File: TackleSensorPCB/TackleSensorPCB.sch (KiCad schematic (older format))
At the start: 26 parts, among them J1 PJ-037A, J2 Conn_01x03_Male, J3 Conn_01x04_Male, J4 Conn_01x07_Male, Q1 2N7002, Q2 2N7002, SW1 SW_DPST_x2, U1 TPS62172DSG, U2 MSP430FR2433IRGER, U3 MMA8452QR1

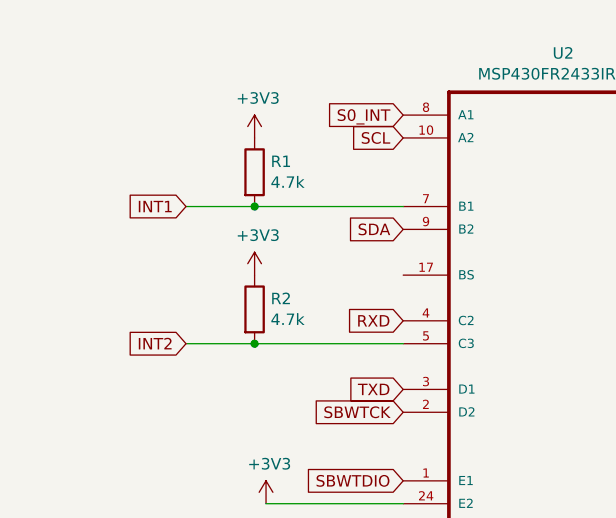
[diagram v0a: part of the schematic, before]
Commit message: Added Footprints
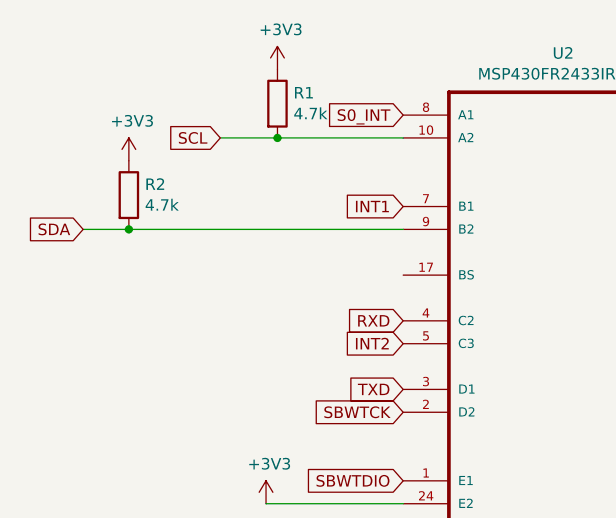
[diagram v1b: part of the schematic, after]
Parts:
- C1, C2, C3, C4, C5: footprint (none) -> Capacitor_SMD:C_0402_1005Metric
- D1: footprint (none) -> LED_SMD:LED_0603_1608Metric
- D2: footprint (none) -> SOD-123FL:SOD123FL
- F1: footprint (none) -> Fuse:Fuse_1206_3216Metric
- J1: footprint CUI_PJ-037A -> PJ-037A:CUI_PJ-037A
- J2: footprint (none) -> Connector_PinHeader_2.54mm:PinHeader_1x03_P2.54mm_Vertical
- J3: footprint (none) -> Connector_PinHeader_2.54mm:PinHeader_1x04_P2.54mm_Vertical
- J4: footprint (none) -> Connector_PinHeader_2.54mm:PinHeader_1x07_P2.54mm_Horizontal
- L1: footprint (none) -> Inductor_SMD:L_0805_2012Metric
- R1, R2, R3, R6, R7: footprint (none) -> Resistor_SMD:R_0402_1005Metric
- R4: footprint (none) -> Resistor_SMD:R_1206_3216Metric
- R5: footprint (none) -> Resistor_SMD:R_0603_1608Metric
- SW1: footprint (none) -> TS-1187A-B-A-B:SW_TS-1187A-B-A-B
- U2: footprint QFN50P400X400X100-25N -> MSP430FR2433:QFN50P400X400X100-25N
- U3: footprint QFN50P300X300X100-16N -> MMA8452QR1:QFN50P300X300X100-16N
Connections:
- net INT1: no longer R1.2
- net INT2: no longer R2.2
- net SCL: now also R1.2
- net SDA: now also R2.2
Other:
- moved on the sheet: R1, R2
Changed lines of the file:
@@
 F 0 "U2" H 2900 3620 50  0000 C CNN
 F 1 "MSP430FR2433IRGER" H 2900 3529 50  0000 C CNN
-F 2 "QFN50P400X400X100-25N" H 2900 2450 50  0001 L BNN
+F 2 "MSP430FR2433:QFN50P400X400X100-25N" H 2900 2450 50  0001 L BNN
 F 3 "" H 2900 2450 50  0001 C CNN
 	1    2900 2450
@@
 F 0 "U3" H 8300 3370 50  0000 C CNN
 F 1 "MMA8452QR1" H 8300 3279 50  0000 C CNN
-F 2 "QFN50P300X300X100-16N" H 8300 2300 50  0001 L BNN
+F 2 "MMA8452QR1:QFN50P300X300X100-16N" H 8300 2300 50  0001 L BNN
 F 3 "Freescale" H 8300 2300 50  0001 L BNN
 F 4 "QFN-16" H 8300 2300 50  0001 L BNN "Field4"
@@
 	1    0    0    -1
 $EndComp
-Text GLabel 1250 2550 0    50   Input ~ 0
+Text GLabel 2200 2550 0    50   Input ~ 0
 INT2
-Text GLabel 1250 1950 0    50   Input ~ 0
+Text GLabel 2200 1950 0    50   Input ~ 0
 INT1
 Text GLabel 2200 1550 0    50   Input ~ 0
 S0_INT
-Text GLabel 2200 2050 0    50   Input ~ 0
+Text GLabel 800  2050 0    50   Input ~ 0
 SDA
-Text GLabel 2200 1650 0    50   Input ~ 0
+Text GLabel 1400 1650 0    50   Input ~ 0
 SCL
 Wire Wire Line
@@
 F 0 "C1" H 2015 4496 50  0000 L CNN
 F 1 "10 uF" H 2015 4405 50  0000 L CNN
-F 2 "" H 1938 4300 50  0001 C CNN
+F 2 "Capacitor_SMD:C_0402_1005Metric" H 1938 4300 50  0001 C CNN
 F 3 "~" H 1900 4450 50  0001 C CNN
 	1    1900 4450
@@
 F 0 "L1" V 3640 4200 50  0000 C CNN
 F 1 "2.2 uH" V 3549 4200 50  0000 C CNN
-F 2 "" H 3450 4200 50  0001 C CNN
+F 2 "Inductor_SMD:L_0805_2012Metric" H 3450 4200 50  0001 C CNN
 F 3 "~" H 3450 4200 50  0001 C CNN
 	1    3450 4200
@@
 F 0 "R3" H 3820 4496 50  0000 L CNN
 F 1 "100k" H 3820 4405 50  0000 L CNN
-F 2 "" V 3680 4450 50  0001 C CNN
+F 2 "Resistor_SMD:R_0402_1005Metric" V 3680 4450 50  0001 C CNN
 F 3 "~" H 3750 4450 50  0001 C CNN
 	1    3750 4450
@@
 INT2
 Wire Wire Line
-	2200 1950 1550 1950
-Wire Wire Line
-	2200 2550 1550 2550
-$Comp
-L Device:R R2
-U 1 1 5F83BDA3
-P 1550 2400
-F 0 "R2" H 1620 2446 50  0000 L CNN
-F 1 "4.7k" H 1620 2355 50  0000 L CNN
-F 2 "" V 1480 2400 50  0001 C CNN
-F 3 "~" H 1550 2400 50  0001 C CNN
-	1    1550 2400
-	1    0    0    -1
-$EndComp
-Connection ~ 1550 2550
-Wire Wire Line
-	1550 2550 1250 2550
+	2200 1650 1650 1650
 $Comp
 L Device:R R1
 U 1 1 5F83C388
-P 1550 1800
-F 0 "R1" H 1620 1846 50  0000 L CNN
-F 1 "4.7k" H 1620 1755 50  0000 L CNN
-F 2 "" V 1480 1800 50  0001 C CNN
-F 3 "~" H 1550 1800 50  0001 C CNN
-	1    1550 1800
-	1    0    0    -1
-$EndComp
-Connection ~ 1550 1950
-Wire Wire Line
-	1550 1950 1250 1950
+P 1650 1500
+F 0 "R1" H 1720 1546 50  0000 L CNN
+F 1 "4.7k" H 1720 1455 50  0000 L CNN
+F 2 "Resistor_SMD:R_0402_1005Metric" V 1580 1500 50  0001 C CNN
+F 3 "~" H 1650 1500 50  0001 C CNN
+	1    1650 1500
+	1    0    0    -1
+$EndComp
 $Comp
 L power:+3V3 #PWR01
 U 1 1 5F83CA3F
-P 1550 1650
-F 0 "#PWR01" H 1550 1500 50  0001 C CNN
-F 1 "+3V3" H 1565 1823 50  0000 C CNN
-F 2 "" H 1550 1650 50  0001 C CNN
-F 3 "" H 1550 1650 50  0001 C CNN
-	1    1550 1650
-	1    0    0    -1
-$EndComp
-$Comp
-L power:+3V3 #PWR02
-U 1 1 5F83D152
-P 1550 2250
-F 0 "#PWR02" H 1550 2100 50  0001 C CNN
-F 1 "+3V3" H 1565 2423 50  0000 C CNN
-F 2 "" H 1550 2250 50  0001 C CNN
-F 3 "" H 1550 2250 50  0001 C CNN
-	1    1550 2250
+P 1650 1350
+F 0 "#PWR01" H 1650 1200 50  0001 C CNN
+F 1 "+3V3" H 1665 1523 50  0000 C CNN
+F 2 "" H 1650 1350 50  0001 C CNN
+F 3 "" H 1650 1350 50  0001 C CNN
+	1    1650 1350
 	1    0    0    -1
 $EndComp
@@
 F 0 "C5" H 7065 2096 50  0000 L CNN
 F 1 "0.1 uF" H 7065 2005 50  0000 L CNN
-F 2 "" H 6988 1900 50  0001 C CNN
+F 2 "Capacitor_SMD:C_0402_1005Metric" H 6988 1900 50  0001 C CNN
 F 3 "~" H 6950 2050 50  0001 C CNN
 	1    6950 2050
@@
 F 0 "D1" V 7939 5932 50  0000 R CNN
 F 1 "LED" V 7848 5932 50  0000 R CNN
-F 2 "" H 7900 6050 50  0001 C CNN
+F 2 "LED_SMD:LED_0603_1608Metric" H 7900 6050 50  0001 C CNN
 F 3 "~" H 7900 6050 50  0001 C CNN
 	1    7900 6050
@@
 F 0 "SW1" H 7700 5535 50  0000 C CNN
 F 1 "SW_DPST_x2" H 7700 5444 50  0000 C CNN
-F 2 "" H 7700 5300 50  0001 C CNN
+F 2 "TS-1187A-B-A-B:SW_TS-1187A-B-A-B" H 7700 5300 50  0001 C CNN
 F 3 "~" H 7700 5300 50  0001 C CNN
 	1    7700 5300
@@
 F 0 "R5" V 7493 4800 50  0000 C CNN
 F 1 "330" V 7584 4800 50  0000 C CNN
-F 2 "" V 7630 4800 50  0001 C CNN
+F 2 "Resistor_SMD:R_0603_1608Metric" V 7630 4800 50  0001 C CNN
 F 3 "~" H 7700 4800 50  0001 C CNN
 	1    7700 4800
@@
 F 0 "J2" H 9908 4331 50  0000 C CNN
 F 1 "Conn_01x03_Male" H 9908 4240 50  0000 C CNN
-F 2 "" H 9800 4050 50  0001 C CNN
+F 2 "Connector_PinHeader_2.54mm:PinHeader_1x03_P2.54mm_Vertical" H 9800 4050 50  0001 C CNN
 F 3 "~" H 9800 4050 50  0001 C CNN
 	1    9800 4050
@@
 F 0 "J4" H 9908 6331 50  0000 C CNN
 F 1 "Conn_01x07_Male" H 9908 6240 50  0000 C CNN
-F 2 "" H 9800 5850 50  0001 C CNN
+F 2 "Connector_PinHeader_2.54mm:PinHeader_1x07_P2.54mm_Horizontal" H 9800 5850 50  0001 C CNN
 F 3 "~" H 9800 5850 50  0001 C CNN
 	1    9800 5850
@@
 F 0 "J1" H 7545 4490 50  0000 C CNN
 F 1 "PJ-037A" H 7545 4399 50  0000 C CNN
-F 2 "CUI_PJ-037A" H 7550 4150 50  0001 L BNN
+F 2 "PJ-037A:CUI_PJ-037A" H 7550 4150 50  0001 L BNN
 F 3 "Manufacturer recommendations" H 7550 4150 50  0001 L BNN
 F 4 "CUI INC" H 7550 4150 50  0001 L BNN "Field4"
@@
 F 0 "R6" H 2870 6096 50  0000 L CNN
 F 1 "4.7k" H 2870 6005 50  0000 L CNN
-F 2 "" V 2730 6050 50  0001 C CNN
+F 2 "Resistor_SMD:R_0402_1005Metric" V 2730 6050 50  0001 C CNN
 F 3 "~" H 2800 6050 50  0001 C CNN
 	1    2800 6050
@@
 F 0 "R7" H 3770 6096 50  0000 L CNN
 F 1 "4.7k" H 3770 6005 50  0000 L CNN
-F 2 "" V 3630 6050 50  0001 C CNN
+F 2 "Resistor_SMD:R_0402_1005Metric" V 3630 6050 50  0001 C CNN
 F 3 "~" H 3700 6050 50  0001 C CNN
 	1    3700 6050
@@
 F 0 "R4" H 7670 6096 50  0000 L CNN
 F 1 "100" H 7670 6005 50  0000 L CNN
-F 2 "" V 7530 6050 50  0001 C CNN
+F 2 "Resistor_SMD:R_1206_3216Metric" V 7530 6050 50  0001 C CNN
 F 3 "~" H 7600 6050 50  0001 C CNN
 	1    7600 6050
@@
 F 0 "C2" H 4315 4496 50  0000 L CNN
 F 1 "10uF" H 4315 4405 50  0000 L CNN
-F 2 "" H 4238 4300 50  0001 C CNN
+F 2 "Capacitor_SMD:C_0402_1005Metric" H 4238 4300 50  0001 C CNN
 F 3 "~" H 4200 4450 50  0001 C CNN
 	1    4200 4450
@@
 F 0 "C3" H 4765 4496 50  0000 L CNN
 F 1 "10uF" H 4765 4405 50  0000 L CNN
-F 2 "" H 4688 4300 50  0001 C CNN
+F 2 "Capacitor_SMD:C_0402_1005Metric" H 4688 4300 50  0001 C CNN
 F 3 "~" H 4650 4450 50  0001 C CNN
 	1    4650 4450
@@
 F 0 "C4" H 5215 4496 50  0000 L CNN
 F 1 "10uF" H 5215 4405 50  0000 L CNN
-F 2 "" H 5138 4300 50  0001 C CNN
+F 2 "Capacitor_SMD:C_0402_1005Metric" H 5138 4300 50  0001 C CNN
 F 3 "~" H 5100 4450 50  0001 C CNN
 	1    5100 4450
@@
 F 0 "F1" H 1300 4385 50  0000 C CNN
 F 1 "Fuse_Small" H 1300 4294 50  0000 C CNN
-F 2 "" H 1300 4200 50  0001 C CNN
+F 2 "Fuse:Fuse_1206_3216Metric" H 1300 4200 50  0001 C CNN
 F 3 "~" H 1300 4200 50  0001 C CNN
 	1    1300 4200
@@
 F 0 "D2" V 1504 4480 50  0000 L CNN
 F 1 "D" V 1595 4480 50  0000 L CNN
-F 2 "" H 1550 4400 50  0001 C CNN
+F 2 "SOD-123FL:SOD123FL" H 1550 4400 50  0001 C CNN
 F 3 "~" H 1550 4400 50  0001 C CNN
 	1    1550 4400
@@
 F 0 "J3" H 9908 5081 50  0000 C CNN
 F 1 "Conn_01x04_Male" H 9908 4990 50  0000 C CNN
-F 2 "" H 9800 4800 50  0001 C CNN
+F 2 "Connector_PinHeader_2.54mm:PinHeader_1x04_P2.54mm_Vertical" H 9800 4800 50  0001 C CNN
 F 3 "~" H 9800 4800 50  0001 C CNN
 	1    9800 4800
@@
 $EndComp
 $Comp
-L power:GND #PWR?
+L power:GND #PWR0101
 U 1 1 5F86DE04
 P 6950 2200
-F 0 "#PWR?" H 6950 1950 50  0001 C CNN
+F 0 "#PWR0101" H 6950 1950 50  0001 C CNN
 F 1 "GND" H 6955 2027 50  0000 C CNN
 F 2 "" H 6950 2200 50  0001 C CNN
@@
 	1    0    0    -1
 $EndComp
+$Comp
+L power:+3V3 #PWR02
+U 1 1 5F83D152
+P 1000 1750
+F 0 "#PWR02" H 1000 1600 50  0001 C CNN
+F 1 "+3V3" H 1015 1923 50  0000 C CNN
+F 2 "" H 1000 1750 50  0001 C CNN
+F 3 "" H 1000 1750 50  0001 C CNN
+	1    1000 1750
+	1    0    0    -1
+$EndComp
+$Comp
+L Device:R R2
+U 1 1 5F83BDA3
+P 1000 1900
+F 0 "R2" H 1070 1946 50  0000 L CNN
+F 1 "4.7k" H 1070 1855 50  0000 L CNN
+F 2 "Resistor_SMD:R_0402_1005Metric" V 930 1900 50  0001 C CNN
+F 3 "~" H 1000 1900 50  0001 C CNN
+	1    1000 1900
+	1    0    0    -1
+$EndComp
+Connection ~ 1000 2050
+Wire Wire Line
+	1000 2050 2200 2050
+Wire Wire Line
+	800  2050 1000 2050
+Wire Wire Line
+	1400 1650 1650 1650
+Connection ~ 1650 1650
 $EndSCHEMATC

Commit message: Created First Revision of PCB
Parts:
- J4: footprint Connector_PinHeader_2.54mm:PinHeader_1x07_P2.54mm_Horizontal -> Connector_PinHeader_2.54mm:PinHeader_1x07_P2.54mm_Vertical
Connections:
- net 3V3 is gone; now on net +3V3: J4.3 (Pin_3)
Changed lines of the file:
@@
 F 0 "J4" H 9908 6331 50  0000 C CNN
 F 1 "Conn_01x07_Male" H 9908 6240 50  0000 C CNN
-F 2 "Connector_PinHeader_2.54mm:PinHeader_1x07_P2.54mm_Horizontal" H 9800 5850 50  0001 C CNN
+F 2 "Connector_PinHeader_2.54mm:PinHeader_1x07_P2.54mm_Vertical" H 9800 5850 50  0001 C CNN
 F 3 "~" H 9800 5850 50  0001 C CNN
 	1    9800 5850
@@
 	1    0    0    -1
 $EndComp
-Text GLabel 10000 5750 2    50   Input ~ 0
-3V3
 Text GLabel 10000 5850 2    50   Input ~ 0
 RXD
@@
 	1400 1650 1650 1650
 Connection ~ 1650 1650
+$Comp
+L power:+3.3V #PWR?
+U 1 1 5F87745C
+P 10150 5750
+F 0 "#PWR?" H 10150 5600 50  0001 C CNN
+F 1 "+3.3V" H 10165 5923 50  0000 C CNN
+F 2 "" H 10150 5750 50  0001 C CNN
+F 3 "" H 10150 5750 50  0001 C CNN
+	1    10150 5750
+	1    0    0    -1
+$EndComp
+Wire Wire Line
+	10000 5750 10150 5750
 $EndSCHEMATC
